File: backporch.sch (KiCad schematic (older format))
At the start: 28 parts, among them J1 MD-90SM, J2 MD-80SM, J3 DB15_Female_HighDensity_Mount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, J4 35RAPC4BH3, U1 EL1883ISZ

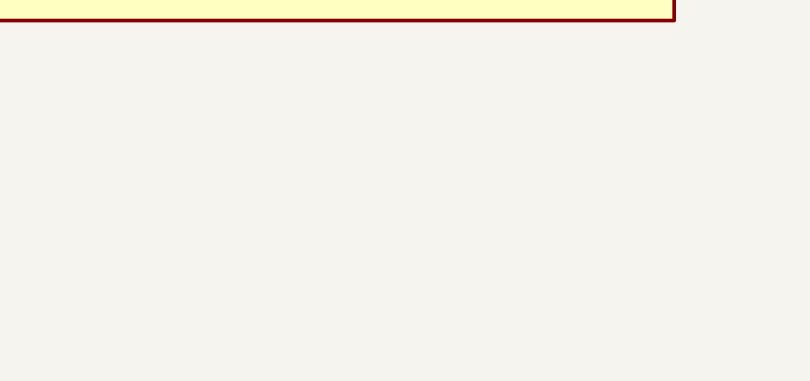
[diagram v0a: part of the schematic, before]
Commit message: Add mounting holes
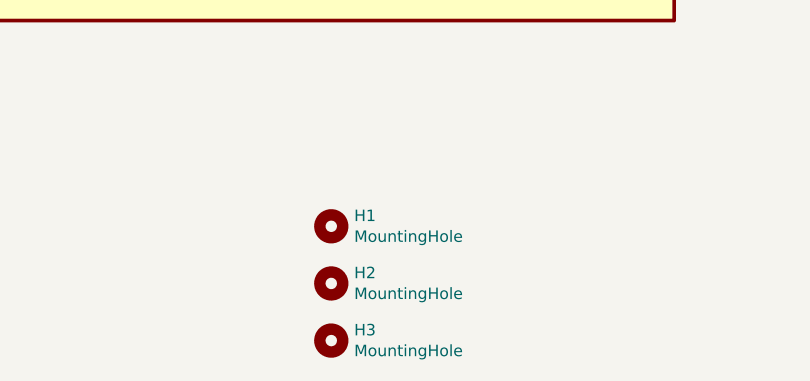
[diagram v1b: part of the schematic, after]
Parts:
- added H1, H2, H3: MountingHole, MountingHole:MountingHole_2.2mm_M2_ISO7380_Pad, symbol Mechanical:MountingHole
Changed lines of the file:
@@
 Wire Wire Line
 	8350 5250 7150 5250
+$Comp
+L Mechanical:MountingHole H1
+U 1 1 60234506
+P 5450 6750
+F 0 "H1" H 5550 6796 50  0000 L CNN
+F 1 "MountingHole" H 5550 6705 50  0000 L CNN
+F 2 "MountingHole:MountingHole_2.2mm_M2_ISO7380_Pad" H 5450 6750 50  0001 C CNN
+F 3 "~" H 5450 6750 50  0001 C CNN
+	1    5450 6750
+	1    0    0    -1
+$EndComp
+$Comp
+L Mechanical:MountingHole H2
+U 1 1 60236289
+P 5450 7000
+F 0 "H2" H 5550 7046 50  0000 L CNN
+F 1 "MountingHole" H 5550 6955 50  0000 L CNN
+F 2 "MountingHole:MountingHole_2.2mm_M2_ISO7380_Pad" H 5450 7000 50  0001 C CNN
+F 3 "~" H 5450 7000 50  0001 C CNN
+	1    5450 7000
+	1    0    0    -1
+$EndComp
+$Comp
+L Mechanical:MountingHole H3
+U 1 1 602362FD
+P 5450 7250
+F 0 "H3" H 5550 7296 50  0000 L CNN
+F 1 "MountingHole" H 5550 7205 50  0000 L CNN
+F 2 "MountingHole:MountingHole_2.2mm_M2_ISO7380_Pad" H 5450 7250 50  0001 C CNN
+F 3 "~" H 5450 7250 50  0001 C CNN
+	1    5450 7250
+	1    0    0    -1
+$EndComp
 $EndSCHEMATC
